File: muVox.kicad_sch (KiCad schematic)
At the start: 42 parts, among them J1 SM10B-SURS-TF, J2 Conn_01x06, J3 Alt.DC, J4 DC IN, J5 IO1, SW1 EG120A, U1 HT7463, U2 XC6220B331MR

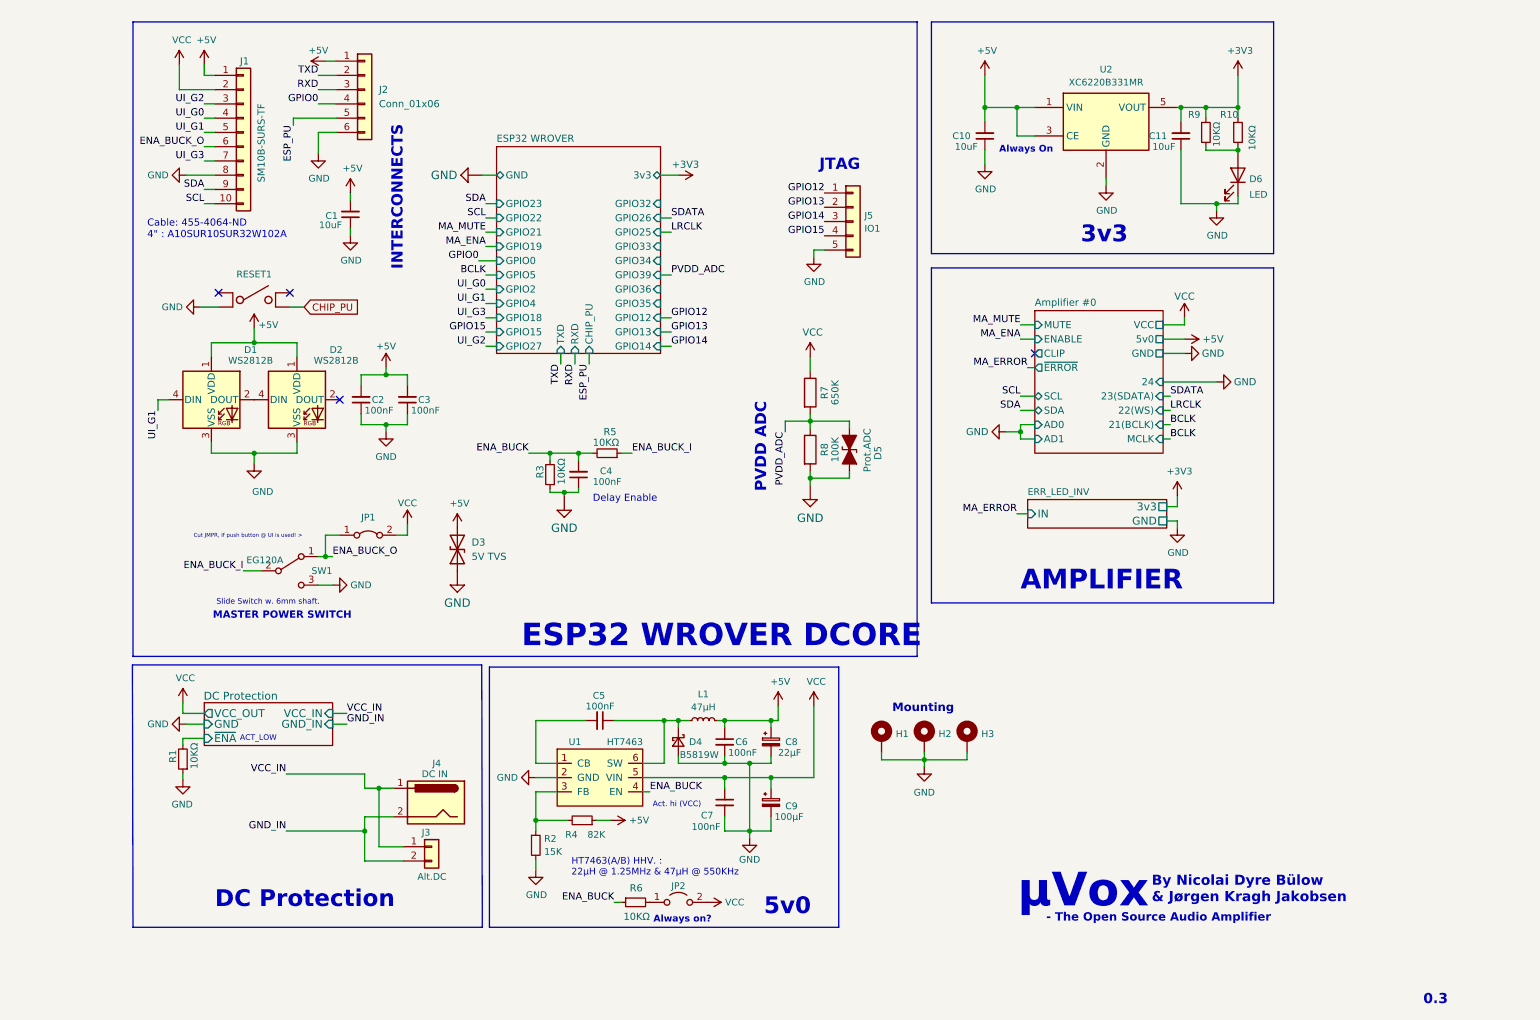
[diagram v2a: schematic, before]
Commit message: Rev04 in the works. New changes include; New DCDC buck, two new connectors, replaced WS-diodes, removed err-diode
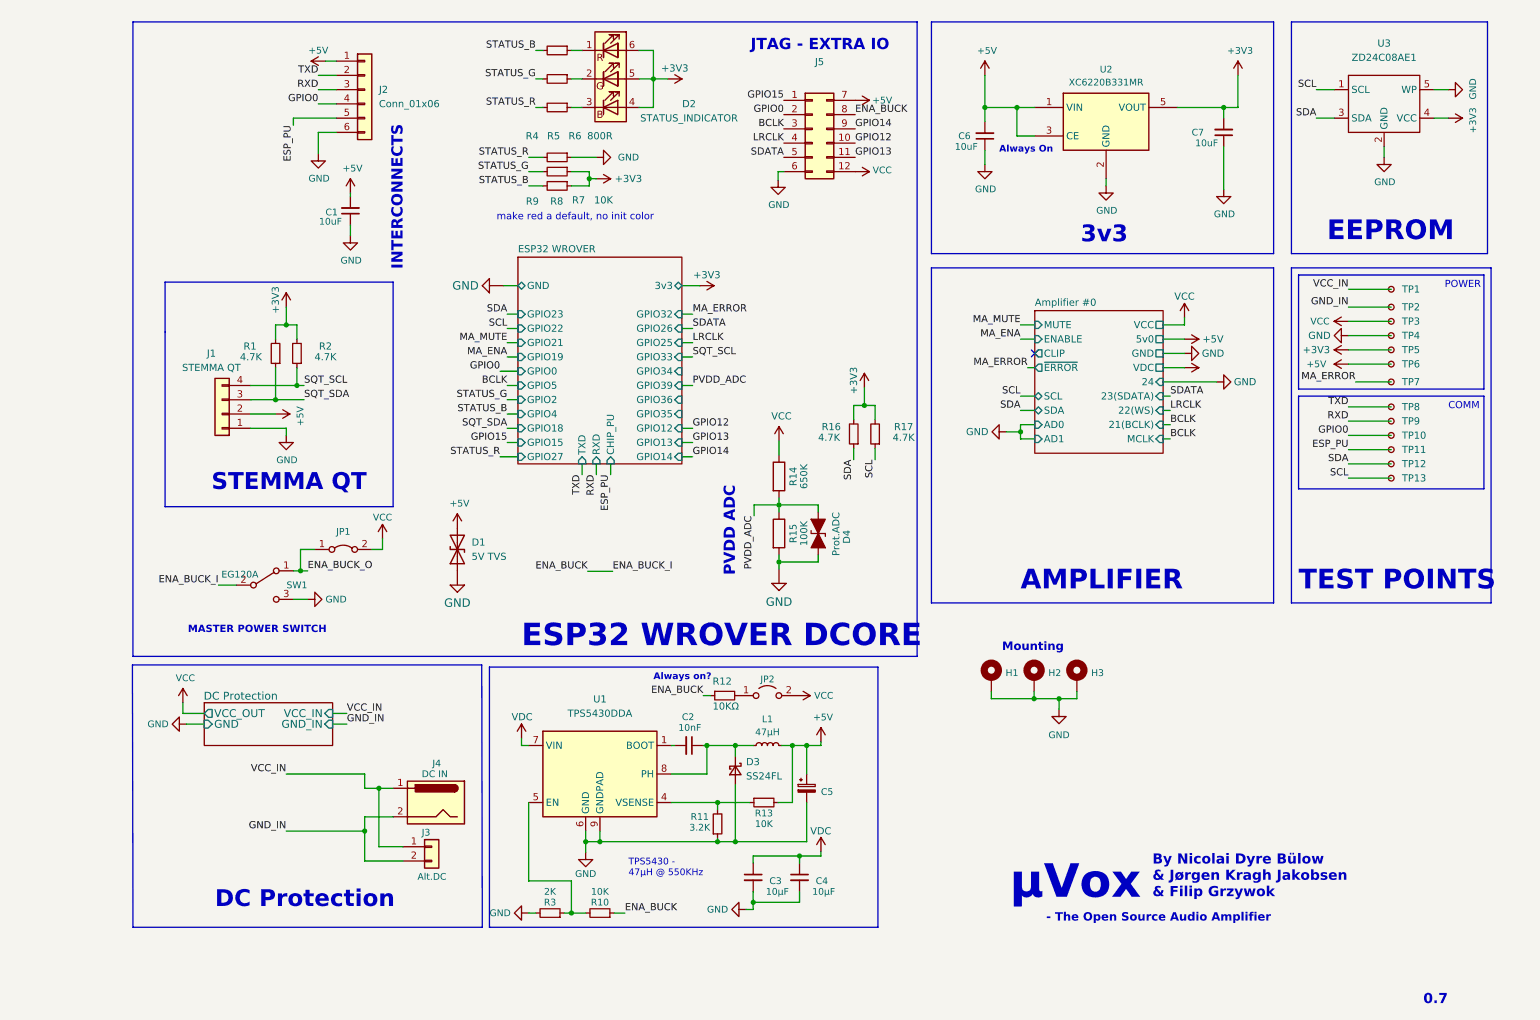
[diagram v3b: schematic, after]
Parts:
- removed C5, C6, C7: 100nF, Capacitor_SMD:C_0603_1608Metric, symbol Device:C_Small
- removed C8: 22µF, Capacitor_SMD:CP_Elec_4x5.4, symbol Device:CP_Small
- removed C9: 100µF, Capacitor_SMD:CP_Elec_8x10, symbol Device:CP_Small
- removed D1, D2: WS2812B, LED_SMD:LED_WS2812B_PLCC4_5.0x5.0mm_P3.2mm, symbol LED:WS2812B
- removed D4: B5819W, Diode_SMD:D_SOD-123, symbol Device:D_Schottky_Small
- removed D6: LED, Diode_SMD:D_0603_1608Metric, symbol Device:LED
- removed J1: SM10B-SURS-TF, Connector_JST:JST_SUR_SM10B-SURS-TF_1x10-1MP_P0.80mm_Horizontal, symbol Connector_Generic:Conn_01x10
- removed J5: IO1, Connector_PinHeader_2.00mm:PinHeader_1x05_P2.00mm_Vertical, symbol Connector_Generic:Conn_01x05
- removed RESET1: SMD_SWITCH, Lib:SMD_SWITCH_SPST_C318801, symbol muVoxSyms:SMD_SWITCH
- removed U1: HT7463, Package_TO_SOT_SMD:SOT-23-6, symbol muVoxSyms:HT7463
- added C5: (no value), symbol Device:CP_Small
- added D2: STATUS_INDICATOR, LED_SMD:LED_WS2812_PLCC6_5.0x5.0mm_P1.6mm, symbol Device:LED_RGB
- added D3: SS24FL, Diode_SMD:D_SMA, symbol Device:D_Schottky_Small
- added J1: STEMMA QT, Connector_JST:JST_SH_SM04B-SRSS-TB_1x04-1MP_P1.00mm_Horizontal, symbol Connector_Generic:Conn_01x04
- added J5: (no value), symbol Connector_Generic:Conn_02x06_Top_Bottom
- added R11: 3.2K, Resistor_SMD:R_0603_1608Metric, symbol Device:R_Small
- added R12: 10KΩ, Resistor_SMD:R_0603_1608Metric, symbol Device:R_Small
- added R13, R7, R8: 10K, Resistor_SMD:R_0603_1608Metric, symbol Device:R_Small
- added R16, R17: 4.7K, Resistor_SMD:R_0603_1608Metric, symbol Device:R_Small
- added TP1, TP10, TP11, TP12, TP13, TP2, TP3, TP4, TP5, TP7, TP8, TP9: TestPoint_Small, TestPoint:TestPoint_Pad_D1.5mm, symbol Connector:TestPoint_Small
- added TP6: (no value), symbol Connector:TestPoint_Small
- added U1: TPS5430DDA, Package_SO:TI_SO-PowerPAD-8_ThermalVias, symbol Regulator_Switching:TPS5430DDA
- added U3: ZD24C08AE1, Package_TO_SOT_SMD:SOT-23-5, symbol Memory_EEPROM:ZD24C08A
- C1: LCSC C15850 -> C162422
- C2: value 100nF -> 10nF; footprint Capacitor_SMD:C_0603_1608Metric -> Capacitor_SMD:C_0805_2012Metric
- C3, C4: value 100nF -> 10µF; footprint Capacitor_SMD:C_0603_1608Metric -> Capacitor_SMD:C_0805_2012Metric; LCSC C30926 -> C440198
- D1: renamed from D3; LCSC C511254 -> C384858
- R1: value 10KΩ -> 4.7K; LCSC C98220 -> (none)
- R10: value 10KΩ -> 10K
- R2: value 15K -> 4.7K; LCSC C328339 -> (none)
- R3: value 10KΩ -> 2K; LCSC C98220 -> C105581
- R4: value 82K -> 800R; LCSC C23254 -> (none)
- R5, R6: value 10KΩ -> 800R; LCSC C98220 -> (none)
- R9: value 10KΩ -> 10K; LCSC C98220 -> (none)
- SW1: Digikey EG1917-ND -> (none); Distributor (none) -> TME; Identifier (none) -> EG1917
- U2: LCSC (none) -> C86534
- renumbered C10 to C6, C11 to C7, D5 to D4, R7 to R14, R8 to R15
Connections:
- net DC Protection/~{ENA} is gone; now on net +3V3: R1.2
- net +3V3: now also R2.2, D2.4 (BA), D2.5 (GA), D2.6 (RA), R16.2, R17.2, R8.1, TP5.1, U3.4 (VCC); no longer R10.1
- net +5V: now also C5.1, J1.2 (Pin_2), J5.7 (Pin_7), R13.2, TP6.1; no longer C2.2, C3.2, R4.1
- net BCLK: now also J5.3 (Pin_3)
- net ENA_BUCK: now also R10.1, SW1.2 (B), J5.8 (Pin_8), R12.1; no longer C4.2, R3.2, R5.2, R6.1
- net ESP_PU: now also TP11.1
- net GND: now also C3.2, C4.2, R3.2, C5.2, D3.2 (A), J1.1 (Pin_1), J5.6 (Pin_6), R11.1, R7.1, TP4.1, U1.6 (GND), U1.9 (GNDPAD), U3.2 (GND), U3.5 (WP); no longer C2.1, C3.1, C4.1, R1.1, R2.2, R3.1
- net GND_IN: now also TP2.1
- net GPIO0: now also J5.2 (Pin_2), TP10.1
- net GPIO12: now also J5.10 (Pin_10)
- net GPIO13: now also J5.11 (Pin_11)
- net GPIO14: now also J5.9 (Pin_9)
- net GPIO15: now also J5.1 (Pin_1)
- net LRCLK: now also J5.4 (Pin_4)
- net MA_ERROR: now also TP7.1
- net RXD: now also TP9.1
- net SCL: now also R17.1, TP13.1, U3.1 (SCL)
- net SDA: now also R16.1, TP12.1, U3.3 (SDA)
- net SDATA: now also J5.5 (Pin_5)
- net TXD: now also TP8.1
- net VCC: now also J5.12 (Pin_12), TP3.1
- net VCC_IN: now also TP1.1
- net SQT_SCL: now reaches R2.1
- net SQT_SCL: now also J1.4 (Pin_4); no longer R4.2
- net at L1.1: now also C2.1, D3.1 (K), U1.8 (PH)
- net at JP2.1 (A): now also R12.2; no longer R6.2
- net at R10.2: now also R3.1, U1.5 (EN); no longer R9.2
- net ENA_BUCK_I: no longer names the net of R5.1
- net ENA_BUCK_I: now also D2.2 (GK); no longer SW1.2 (B)
- new net: R11.2, R13.1, U1.4 (VSENSE)
- new net: C2.2, U1.1 (BOOT)
- new net: D2.3 (BK), R6.1
- new net: D2.1 (RK), R4.1
- new net SQT_SDA: J1.3 (Pin_3), R1.1
- new net STATUS_B: R4.2, R9.2
- new net STATUS_G: R5.2, R8.2
- new net STATUS_R: R6.2, R7.2
- new net VDC: C3.1, C4.1, U1.7 (VIN)
- no-connect marks 4 -> 1
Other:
- removed sheet ERR_LED_INV
- sheet Amplifier #0 ports: added VDC; removed none
- sheet DC Protection ports: added none; removed ~{ENA}
- note added: "0.7"
- note added: "By Nicolai Dyre Bülow & Jørgen Kragh Jakobsen & Filip Grzywok"
- note added: "COMM"
- note added: "EEPROM"
- note added: "JTAG - EXTRA IO"
- note added: "POWER"
- note added: "STEMMA QT"
- note added: "TEST POINTS"
- note added: "TPS5430 - 47µH @ 550KHz"
- note added: "make red a default, no init color"
- note removed: "0.3"
- note removed: "5v0"
- note removed: "ACT_LOW"
- note removed: "Act. hi (VCC)"
- note removed: "By Nicolai Dyre Bülow & Jørgen Kragh Jakobsen"
- note removed: "Cable: 455-4064-ND 4" : A10SUR10SUR32W102A"
- note removed: "Cut JMPR, If push button @ UI is used! >"
- note removed: "Delay Enable"
- note removed: "HT7463(A/B) HHV. : 22µH @ 1.25MHz & 47µH @ 550KHz"
- note removed: "JTAG"
- note removed: "Slide Switch w. 6mm shaft."
- moved on the sheet: C1, C7, D4, H1, H2, H3, JP1, R14, R15, SW1

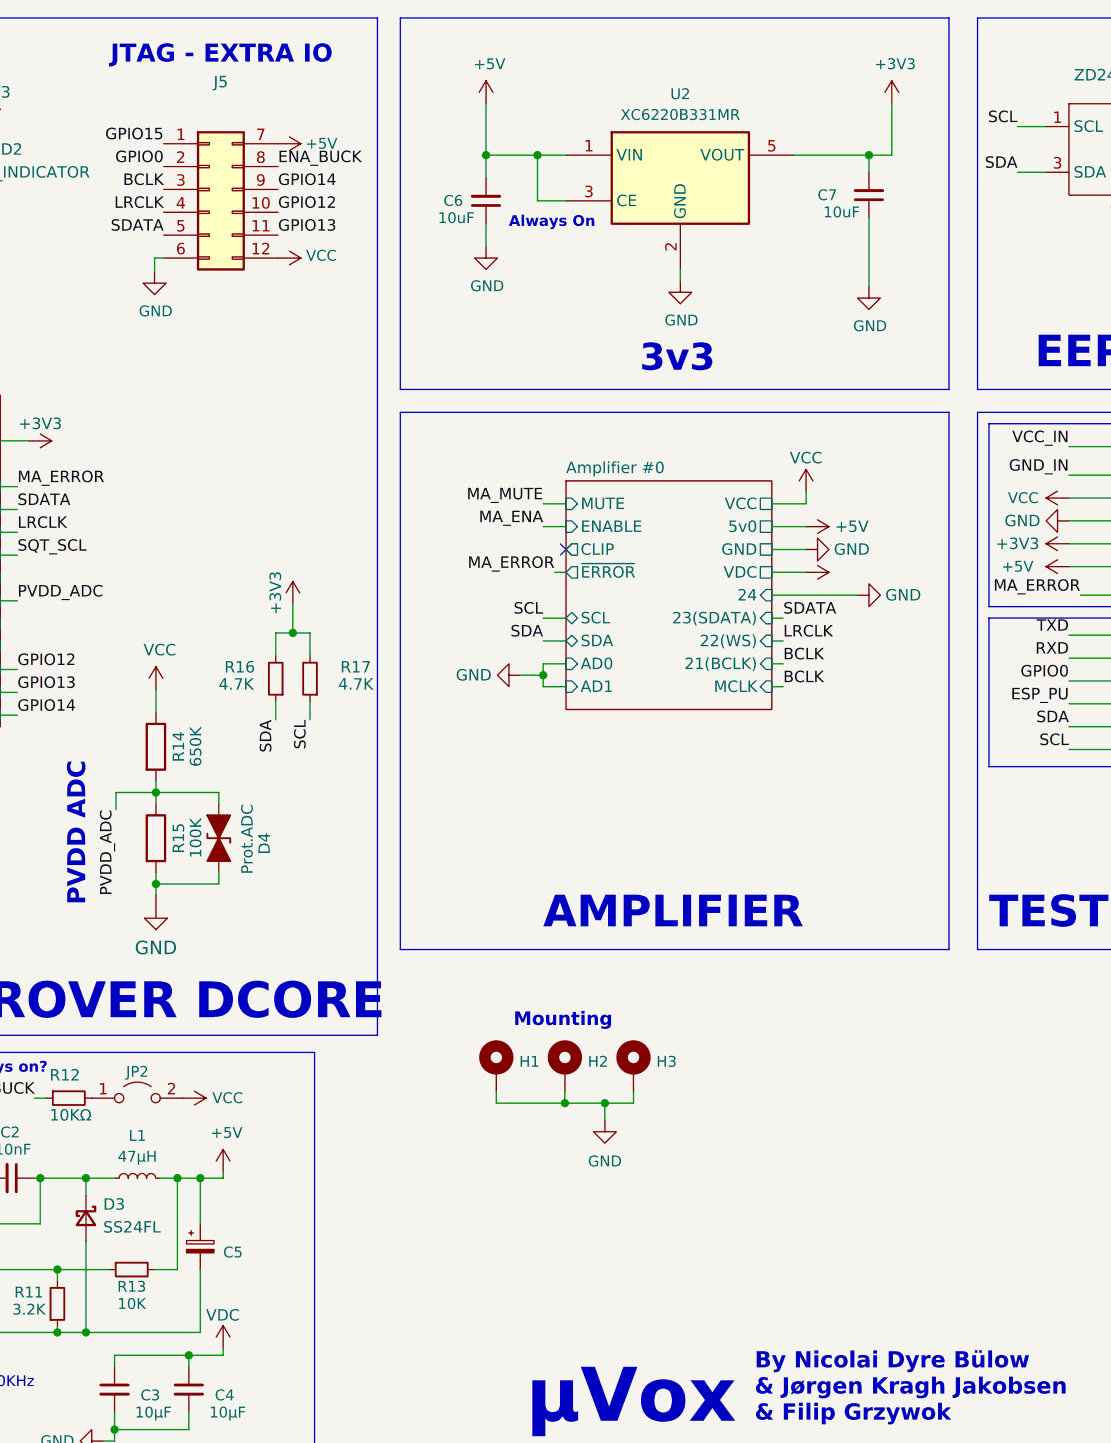
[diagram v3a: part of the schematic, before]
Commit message: fix: Drop voltage on error pin, for mcu read
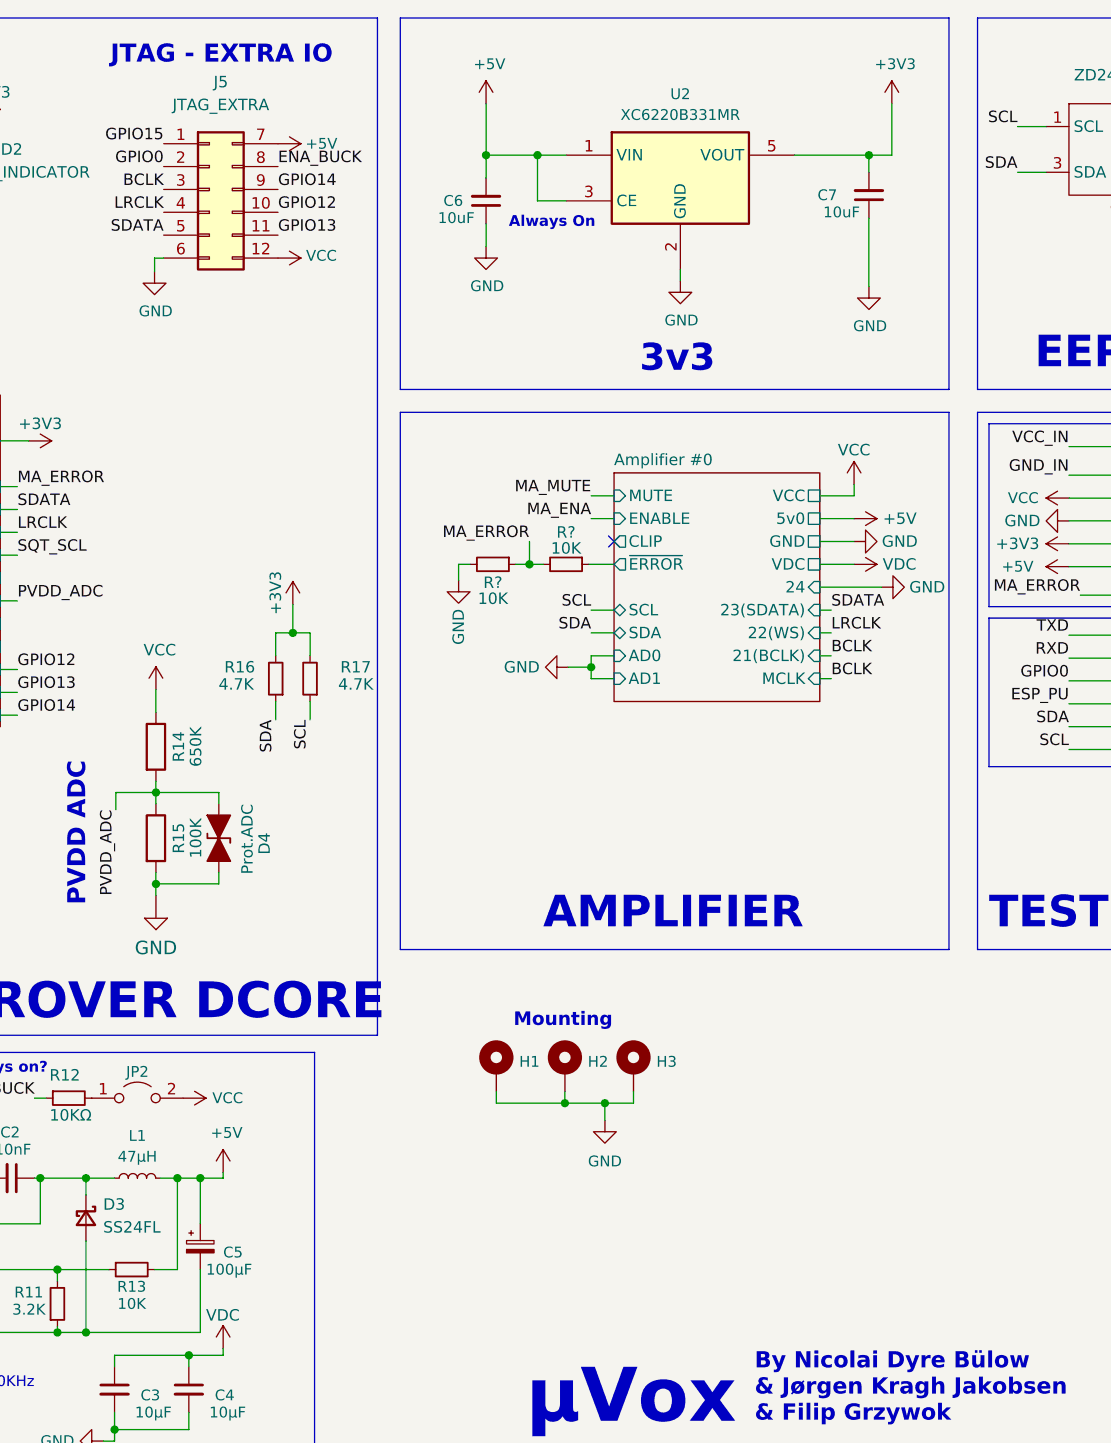
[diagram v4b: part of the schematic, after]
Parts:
- added R? (x2): 10K, Resistor_SMD:R_0603_1608Metric, symbol Device:R_Small
- C5: value (none) -> 100µF; footprint (none) -> Capacitor_SMD:C_Elec_5x5.4
- J5: value (none) -> JTAG_EXTRA; footprint (none) -> Connector_IDC:IDC-Header_2x06_P2.54mm_Vertical
- TP6: value (none) -> TestPoint_Small; footprint (none) -> TestPoint:TestPoint_Pad_D1.5mm
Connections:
- net GND: now also R?.2
- net MA_ERROR: now also R?.1, R?.2
- new net Amplifier #0/~{ERROR}: R?.1
